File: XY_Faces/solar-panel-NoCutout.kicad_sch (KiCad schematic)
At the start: 25 parts, among them J1 CON-5040500591, J2 Conn_01x01, J3 Conn_01x01, J4 Conn_01x01, J5 Conn_01x01, U1 VEML7700, U2 MCP9808_DFN, U3 DRV2605LDGS

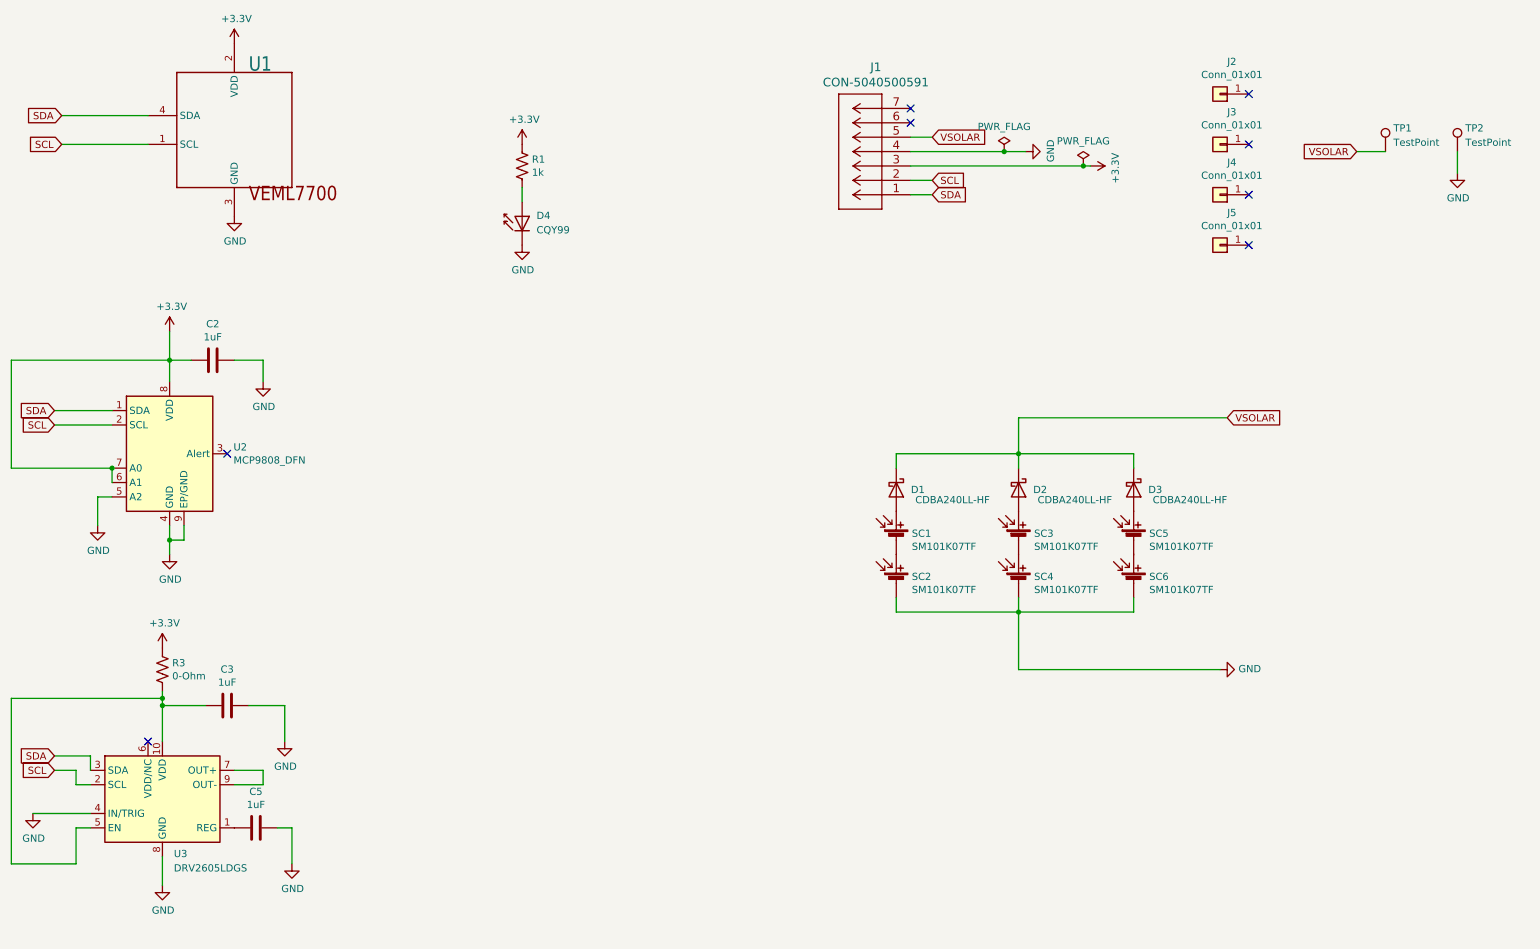
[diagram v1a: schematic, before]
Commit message: removed coil wires, may have power conenctions that need to be removed and etc
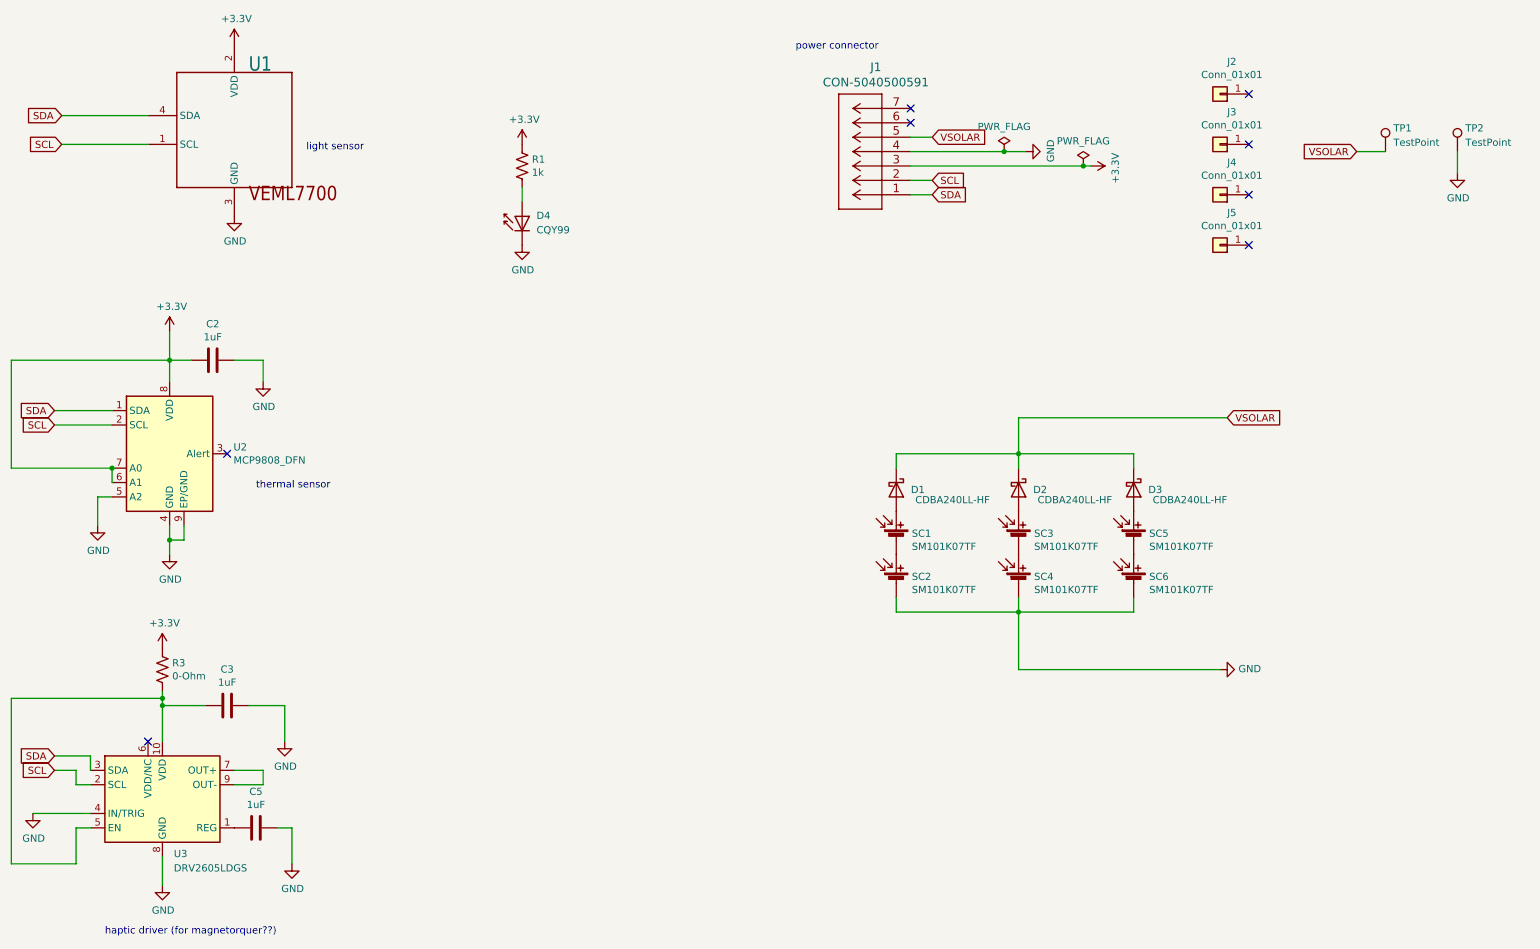
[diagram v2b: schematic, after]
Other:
- note added: "haptic driver (for magnetorquer??)"
- note added: "light sensor"
- note added: "power connector"
- note added: "thermal sensor"
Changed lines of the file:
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@@
     (stroke (width 0) (type default))
+  )
+  (text "light sensor" (at 69.85 44.45 0)
+    (effects (font (size 1.27 1.27)) (justify left bottom))
+  )
+  (text "power connector" (at 156.21 26.67 0)
+    (effects (font (size 1.27 1.27)) (justify left bottom))
+  )
+  (text "haptic driver (for magnetorquer??)" (at 34.29 182.88 0)
+    (effects (font (size 1.27 1.27)) (justify left bottom))
+  )
+  (text "thermal sensor" (at 60.96 104.14 0)
+    (effects (font (size 1.27 1.27)) (justify left bottom))
   )
   (global_label "VSOLAR" (shape input) (at 232.41 91.44 0) (fields_autoplaced)
